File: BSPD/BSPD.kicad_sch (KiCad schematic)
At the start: 40 parts, among them J1 DT13-48PABCD-R015, K1 Latching Relay, Q1 STS6NF20V, U1 LM7805CT, U10 DK1A1B-12V, U12 LM555N, U2 NSL-32, U2 OP AMP, U3 OP AMP, U4 Inverter (Not Gate), U5 2x4 OR GATE, U6 LM555N, U8 NAND, U9 AND GATE

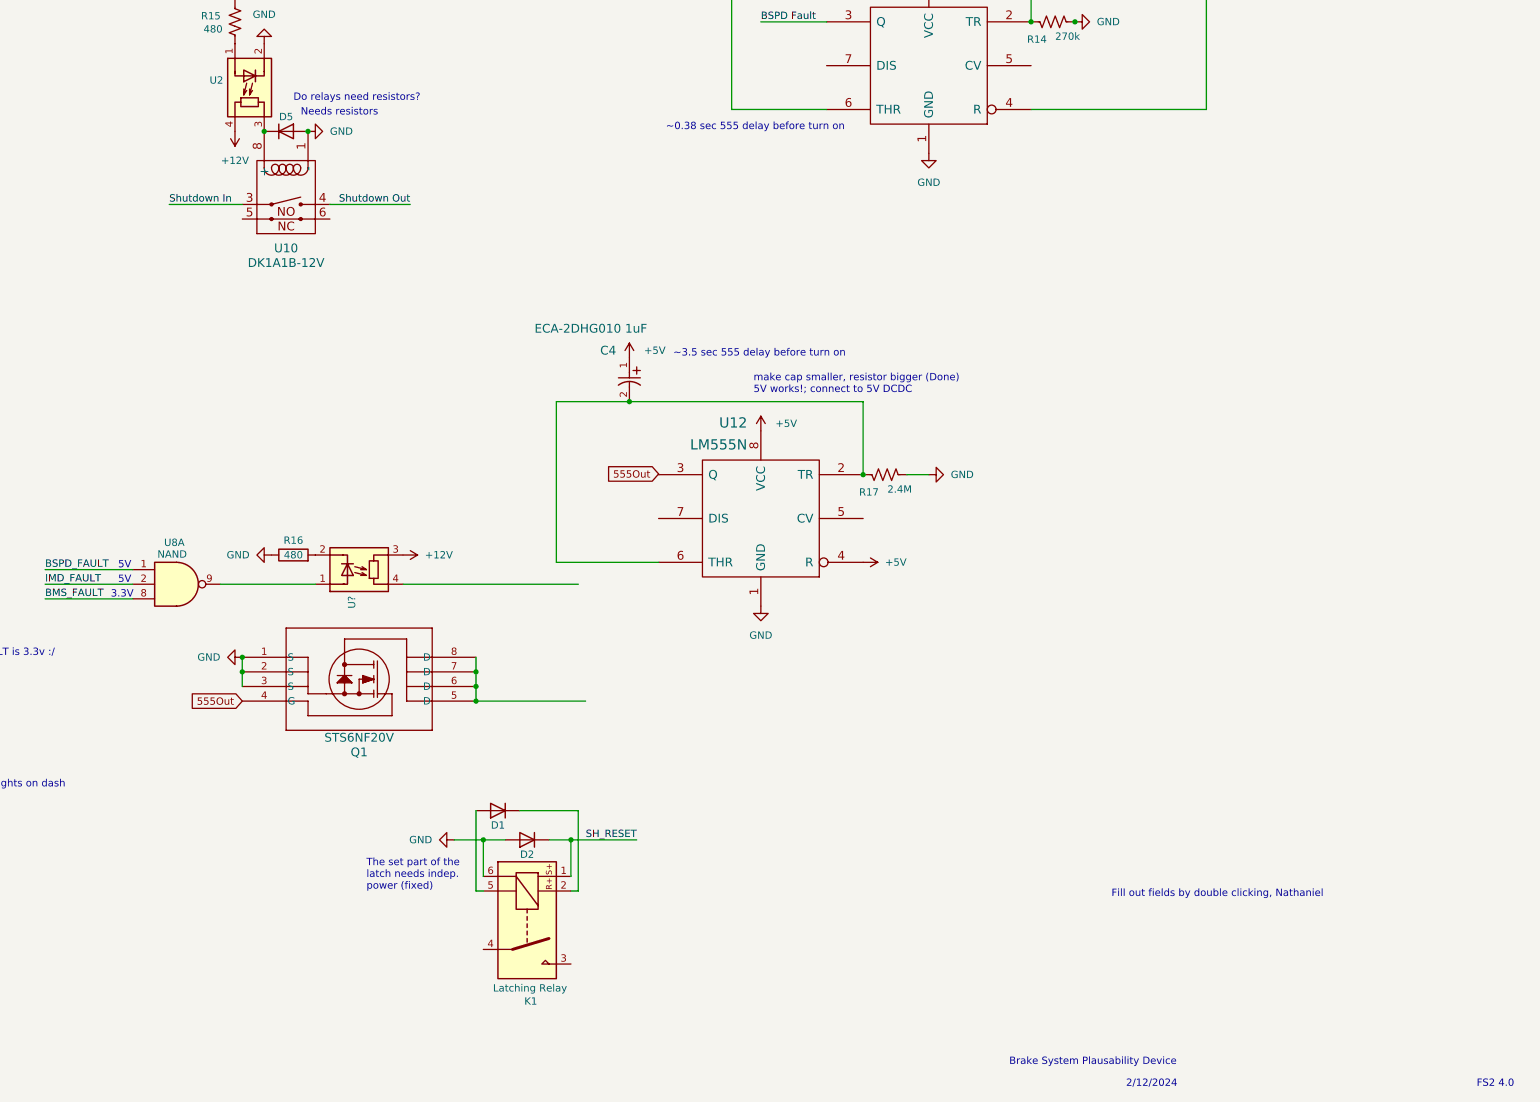
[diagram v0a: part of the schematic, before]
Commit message: Merge branch 'master' of github.com:formulaslug/fs-2-schematics
Updated title to be in title text rather than text
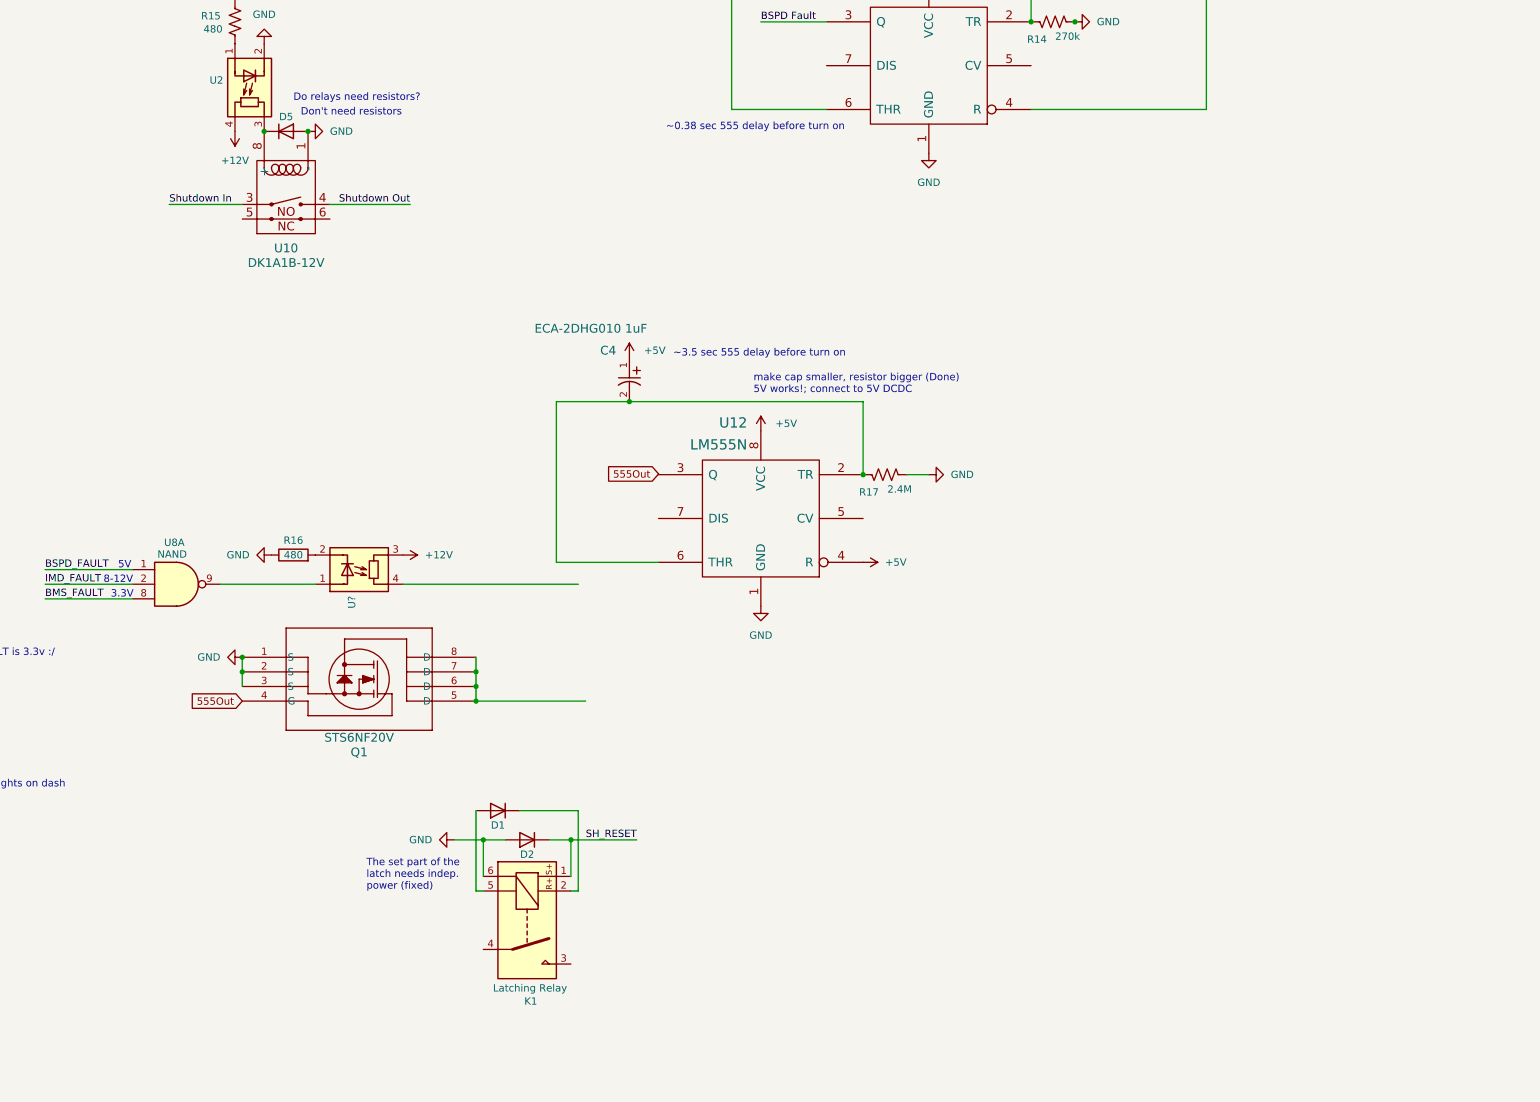
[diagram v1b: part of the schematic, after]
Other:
- note added: "8-12V"
- note added: "Don't need resistors"
- note removed: "2/12/2024"
- note removed: "Brake System Plausability Device"
- note removed: "FS2 4.0"
- note removed: "Fill out fields by double clicking, Nathaniel"
- note removed: "Needs resistors"
- title: (none) -> Brake System Plausability Device
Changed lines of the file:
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@@
 (kicad_sch (version 20230121) (generator eeschema)
   (paper "A3")
+  (title_block
+    (title "Brake System Plausability Device")
+    (date "2024-02-22")
+    (rev "FS2 4.1")
+  )
   (junction (at 45.72 34.29) (diameter 0) (color 0 0 0 0)
   )
@@
     (effects (font (size 1.27 1.27)) (justify left bottom))
   )
-  (text "Fill out fields by double clicking, Nathaniel" (at 326.39 247.65 0)
-    (effects (font (size 1.27 1.27)) (justify left bottom))
-  )
   (text "GLV" (at 46.101 145.796 0)
     (effects (font (size 1.27 1.27)) (justify left bottom))
@@
     (effects (font (size 1.27 1.27)) (justify left bottom))
   )
-  (text "5V" (at 153.67 193.04 0)
+  (text "8-12V" (at 151.13 193.04 0)
     (effects (font (size 1.27 1.27)) (justify left bottom))
   )
@@
     (effects (font (size 1.27 1.27)) (justify left bottom))
   )
-  (text "Needs resistors\n" (at 185.42 111.76 0)
-    (effects (font (size 1.27 1.27)) (justify left bottom))
-  )
-  (text "2/12/2024" (at 328.93 280.67 0)
+  (text "Don't need resistors\n" (at 185.42 111.76 0)
     (effects (font (size 1.27 1.27)) (justify left bottom))
   )
@@
     (effects (font (size 1.27 1.27)) (justify left bottom))
   )
-  (text "Brake System Plausability Device" (at 308.61 276.86 0)
-    (effects (font (size 1.27 1.27)) (justify left bottom))
-  )
   (text "GND" (at 46.101 148.336 0)
     (effects (font (size 1.27 1.27)) (justify left bottom))
@@
     (effects (font (size 1.27 1.27)) (justify left bottom))
   )
-  (text "FS2 4.0\n" (at 389.89 280.67 0)
-    (effects (font (size 1.27 1.27)) (justify left bottom))
-  )

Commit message: Update BSPD.kicad_sch
bspd upadtes
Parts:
- added C5, C6: C_Polarized, 1FS_2_Global_Footprint_Library:Basic 2 Hole, symbol Device:C_Polarized
- added U13: LM7805CT, 1FS_2_Global_Footprint_Library:Basic 3 Hole, symbol Regulator_Linear:LM317_TO-252
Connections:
- net GND: now also C5.2, C6.2, U13.1 (ADJ)
- net IMD_FAULT: now also C5.1, U13.3 (VI); no longer U8.2
- new net: C6.1, U13.2 (VO), U8.2
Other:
- note added: "IMD_FAULT 5V"
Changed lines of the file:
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@@
     (rev "FS2 4.1")
   )
+  (junction (at 93.98 193.04) (diameter 0) (color 0 0 0 0)
+  )
   (junction (at 45.72 34.29) (diameter 0) (color 0 0 0 0)
   )
@@
   )
   (junction (at 320.04 95.25) (diameter 0) (color 0 0 0 0)
+  )
+  (junction (at 115.57 193.04) (diameter 0) (color 0 0 0 0)
+  )
+  (junction (at 104.14 200.66) (diameter 0) (color 0 0 0 0)
   )
   (junction (at 298.45 71.12) (diameter 0) (color 0 0 0 0)
@@
     (stroke (width 0) (type default))
   )
-  (wire (pts (xy 140.97 193.04) (xy 156.21 193.04))
+  (wire (pts (xy 115.57 193.04) (xy 156.21 193.04))
     (stroke (width 0) (type default))
   )
@@
     (stroke (width 0) (type default))
   )
+  (wire (pts (xy 74.93 193.04) (xy 93.98 193.04))
+    (stroke (width 0) (type default))
+  )
   (wire (pts (xy 220.98 237.49) (xy 217.17 237.49))
     (stroke (width 0) (type default))
@@
     (stroke (width 0) (type default))
   )
+  (wire (pts (xy 111.76 193.04) (xy 115.57 193.04))
+    (stroke (width 0) (type default))
+  )
   (wire (pts (xy 215.9 213.36) (xy 234.95 213.36))
     (stroke (width 0) (type default))
@@
     (stroke (width 0) (type default))
   )
+  (wire (pts (xy 93.98 193.04) (xy 96.52 193.04))
+    (stroke (width 0) (type default))
+  )
   (wire (pts (xy 265.43 95.25) (xy 276.86 95.25))
     (stroke (width 0) (type default))
@@
     (stroke (width 0) (type default))
   )
+  (wire (pts (xy 104.14 200.66) (xy 115.57 200.66))
+    (stroke (width 0) (type default))
+  )
   (wire (pts (xy 204.47 127) (xy 190.5 127))
     (stroke (width 0) (type default))
@@
   )
   (wire (pts (xy 164.211 67.31) (xy 167.64 67.31))
+    (stroke (width 0) (type default))
+  )
+  (wire (pts (xy 93.98 200.66) (xy 104.14 200.66))
     (stroke (width 0) (type default))
   )
@@
     (effects (font (size 1.27 1.27)) (justify left bottom))
   )
-  (text "8-12V" (at 151.13 193.04 0)
+  (text "8-12V" (at 86.36 193.04 0)
     (effects (font (size 1.27 1.27)) (justify left bottom))
   )
@@
     (effects (font (size 1.27 1.27)) (justify left bottom))
   )
-  (text "BMS_FAULT is 3.3v :/" (at 124.46 205.74 0)
-    (effects (font (size 1.27 1.27)) (justify left bottom))
-  )
-  (text "Current Sensor\nOpen Circuit\n" (at 97.79 121.92 0)
+  (text "BMS_FAULT is 3.3v :/" (at 137.16 198.12 0)
+    (effects (font (size 1.27 1.27)) (justify left bottom))
+  )
+  (text "Current Sensor\nOpen Circuit\n" (at 92.71 127 0)
     (effects (font (size 1.27 1.27)) (justify left bottom))
   )
@@
   )
   (text "BSPD delay (0.5 sec)" (at 300.99 74.93 0)
+    (effects (font (size 1.27 1.27)) (justify left bottom))
+  )
+  (text "IMD_FAULT 5V" (at 118.11 193.04 0)
+    (effects (font (size 1.27 1.27)) (justify left bottom))
+  )
+  (text "IMD_FAULT 5V" (at 142.24 193.04 0)
     (effects (font (size 1.27 1.27)) (justify left bottom))
   )
@@
     (effects (font (size 1.27 1.27)) (justify left bottom))
   )
-  (label "IMD_FAULT" (at 140.97 193.04 0) (fields_autoplaced)
-    (effects (font (size 1.27 1.27)) (justify left bottom))
-  )
   (label "BSPD_FAULT" (at 140.97 190.5 0) (fields_autoplaced)
+    (effects (font (size 1.27 1.27)) (justify left bottom))
+  )
+  (label "IMD_FAULT" (at 74.93 193.04 0) (fields_autoplaced)
     (effects (font (size 1.27 1.27)) (justify left bottom))
   )
@@
     )
   )
+  (symbol (lib_id "power:GND") (at 104.14 200.66 0) (unit 1)
+    (in_bom yes) (on_board yes) (dnp no) (fields_autoplaced)
+    (property "Reference" "#PWR042" (at 104.14 207.01 0)
+      (effects (font (size 1.27 1.27)) hide)
+    )
+    (property "Value" "GND" (at 104.14 205.74 0)
+      (effects (font (size 1.27 1.27)))
+    )
+    (property "Footprint" "" (at 104.14 200.66 0)
+      (effects (font (size 1.27 1.27)) hide)
+    )
+    (property "Datasheet" "" (at 104.14 200.66 0)
+      (effects (font (size 1.27 1.27)) hide)
+    )
+    (pin "1")
+    (instances
+      (project "BSPD"
+        (path "/9b958334-fa88-4811-8197-71444a07b1b5"
+          (reference "#PWR042") (unit 1)
+        )
+      )
+    )
+  )
   (symbol (lib_id "Regulator_Linear:LM317_TO-252") (at 34.29 34.29 0) (unit 1)
     (in_bom yes) (on_board yes) (dnp no) (fields_autoplaced)
@@
     )
   )
+  (symbol (lib_id "Regulator_Linear:LM317_TO-252") (at 104.14 193.04 0) (unit 1)
+    (in_bom yes) (on_board yes) (dnp no) (fields_autoplaced)
+    (property "Reference" "U13" (at 104.14 186.69 0)
+      (effects (font (size 1.27 1.27)))
+    )
+    (property "Value" "LM7805CT" (at 104.14 189.23 0)
+      (effects (font (size 1.27 1.27)))
+    )
+    (property "Footprint" "1FS_2_Global_Footprint_Library:Basic 3 Hole" (at 104.14 186.69 0)
+      (effects (font (size 1.27 1.27) italic) hide)
+    )
+    (property "Datasheet" "https://www.ti.com/lit/ds/symlink/lm7800.pdf" (at 104.14 193.04 0)
+      (effects (font (size 1.27 1.27)) hide)
+    )
+    (pin "1")
+    (pin "2")
+    (pin "3")
+    (instances
+      (project "BSPD"
+        (path "/9b958334-fa88-4811-8197-71444a07b1b5"
+          (reference "U13") (unit 1)
+        )
+      )
+    )
+  )
   (symbol (lib_id "Device:R_US") (at 35.56 93.98 270) (unit 1)
     (in_bom yes) (on_board yes) (dnp no)
@@
         (path "/e19d26dd-723b-45e6-9d59-b1730158e759"
           (reference "#PWR024") (unit 1)
+        )
+      )
+    )
+  )
+  (symbol (lib_id "Device:C_Polarized") (at 93.98 196.85 0) (unit 1)
+    (in_bom yes) (on_board yes) (dnp no)
+    (property "Reference" "C5" (at 88.9 199.39 0)
+      (effects (font (size 1.27 1.27)) (justify left))
+    )
+    (property "Value" "C_Polarized" (at 88.9 201.93 0)
+      (effects (font (size 1.27 1.27)) (justify left))
+    )
+    (property "Footprint" "1FS_2_Global_Footprint_Library:Basic 2 Hole" (at 94.9452 200.66 0)
+      (effects (font (size 1.27 1.27)) hide)
+    )
+    (property "Datasheet" "~" (at 93.98 196.85 0)
+      (effects (font (size 1.27 1.27)) hide)
+    )
+    (pin "1")
+    (pin "2")
+    (instances
+      (project "BSPD"
+        (path "/9b958334-fa88-4811-8197-71444a07b1b5"
+          (reference "C5") (unit 1)
         )
       )
@@
         )
       )
+    )
+  )
+  (symbol (lib_id "Device:C_Polarized") (at 115.57 196.85 0) (unit 1)
+    (in_bom yes) (on_board yes) (dnp no) (fields_autoplaced)
+    (property "Reference" "C6" (at 119.38 194.691 0)
+      (effects (font (size 1.27 1.27)) (justify left))
+    )
+    (property "Value" "C_Polarized" (at 119.38 197.231 0)
+      (effects (font (size 1.27 1.27)) (justify left))
+    )
+    (property "Footprint" "1FS_2_Global_Footprint_Library:Basic 2 Hole" (at 116.5352 200.66 0)
+      (effects (font (size 1.27 1.27)) hide)
+    )
+    (property "Datasheet" "~" (at 115.57 196.85 0)
+      (effects (font (size 1.27 1.27)) hide)
+    )
+    (pin "1")
+    (pin "2")
+    (instances
+      (project "BSPD"
+        (path "/9b958334-fa88-4811-8197-71444a07b1b5"
+          (reference "C6") (unit 1)
+        )
+      )

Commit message: Updated for Mosfet, latching, and dash lights
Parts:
- removed CR2: STS6NF20V, 1FS_2_Global_Footprint_Library:SO-8_STM, symbol 1_ACC_BOARD:STS6NF20V
- removed R13: 8.2k, Resistor_THT:R_Axial_DIN0207_L6.3mm_D2.5mm_P10.16mm_Horizontal, symbol Device:R_US
- removed R16: 480, symbol Device:R
- removed R7: 100k, Resistor_THT:R_Axial_DIN0207_L6.3mm_D2.5mm_P10.16mm_Horizontal, symbol Device:R_US
- added Q2, Q3: STS6NF20V, 1FS_2_Global_Footprint_Library:SO-8_STM, symbol 1_ACC_BOARD:STS6NF20V
- C3: footprint PCAP_63x112_PAN -> 1FS_2_Global_Footprint_Library:PCAP_63x112_PAN
- R1: value 20k -> 39k; footprint Resistor_THT:R_Axial_DIN0207_L6.3mm_D2.5mm_P10.16mm_Horizontal -> Resistor_SMD:R_0805_2012Metric_Pad1.20x1.40mm_HandSolder
- R10: value 100k -> 330k; footprint Resistor_THT:R_Axial_DIN0207_L6.3mm_D2.5mm_P10.16mm_Horizontal -> Resistor_SMD:R_0805_2012Metric_Pad1.20x1.40mm_HandSolder
- R11: value 3k -> 39k; footprint Resistor_THT:R_Axial_DIN0207_L6.3mm_D2.5mm_P10.16mm_Horizontal -> Resistor_SMD:R_0805_2012Metric_Pad1.20x1.40mm_HandSolder
- R12: value 22k -> 15k; footprint Resistor_THT:R_Axial_DIN0207_L6.3mm_D2.5mm_P10.16mm_Horizontal -> Resistor_SMD:R_0805_2012Metric_Pad1.20x1.40mm_HandSolder
- R14, R3: footprint Resistor_THT:R_Axial_DIN0207_L6.3mm_D2.5mm_P10.16mm_Horizontal -> Resistor_SMD:R_0805_2012Metric_Pad1.20x1.40mm_HandSolder
- R15: value 480 -> 470; footprint Resistor_THT:R_Axial_DIN0207_L6.3mm_D2.5mm_P10.16mm_Horizontal -> Resistor_SMD:R_0805_2012Metric_Pad1.20x1.40mm_HandSolder
- R17: footprint (none) -> Resistor_SMD:R_0805_2012Metric_Pad1.20x1.40mm_HandSolder
- R2: value 10k -> 18k; footprint Resistor_THT:R_Axial_DIN0207_L6.3mm_D2.5mm_P10.16mm_Horizontal -> Resistor_SMD:R_0805_2012Metric_Pad1.20x1.40mm_HandSolder
- R4: value 22k -> 18k; footprint Resistor_THT:R_Axial_DIN0207_L6.3mm_D2.5mm_P10.16mm_Horizontal -> Resistor_SMD:R_0805_2012Metric_Pad1.20x1.40mm_HandSolder
- R5: value 100k -> 82k; footprint Resistor_THT:R_Axial_DIN0207_L6.3mm_D2.5mm_P10.16mm_Horizontal -> Resistor_SMD:R_0805_2012Metric_Pad1.20x1.40mm_HandSolder
- R6: value 75k -> 470; footprint Resistor_THT:R_Axial_DIN0207_L6.3mm_D2.5mm_P10.16mm_Horizontal -> Resistor_SMD:R_0805_2012Metric_Pad1.20x1.40mm_HandSolder
- R8: value 11k -> 330k; footprint Resistor_THT:R_Axial_DIN0207_L6.3mm_D2.5mm_P10.16mm_Horizontal -> Resistor_SMD:R_0805_2012Metric_Pad1.20x1.40mm_HandSolder
- R9: value 100k -> 10k; footprint Resistor_THT:R_Axial_DIN0207_L6.3mm_D2.5mm_P10.16mm_Horizontal -> Resistor_SMD:R_0805_2012Metric_Pad1.20x1.40mm_HandSolder
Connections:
- net BMS_FAULT is gone; now on net BMS_FAULT 5V: U8.8
- net +12V: now also U?.4 (R); no longer U?.3 (R)
- net +5V: now also R1.1, R9.2; no longer R12.1, R8.1
- net 4.5V: now also R1.2, R8.1; no longer R8.2, R9.1
- net GND: now also J1.D1, R11.2, R12.1, R3.1, R6.1, R8.2, Q2.1 (S), Q2.2 (S), Q2.3 (S), Q3.1 (S), Q3.2 (S), Q3.3 (S); no longer J1.A2, R1.1, R9.2
- net IMD_FAULT: now also J1.A9
- net SH_RESET: now also J1.A6
- net Shutdown In: now also J1.A8; no longer J1.A5
- net Shutdown Out: now also J1.D3, K1.3; no longer J1.A6, U10.4
- net at C3.1, U6.4 (R), U6.8 (VCC): now also U4.4
- net BMS_FAULT 3.3V: now reaches U3.10
- net BMS_FAULT 3.3V: now also J1.A10
- net BMS_FAULT 5V: now reaches U3.8
- net BMS_FAULT 5V: now also Q2.4 (G)
- net 3V: now reaches U3.9
- net 3V: now also R12.2, R9.1
- net at D1.1 (K), K1.2: now also Q1.5 (D), Q1.6 (D), Q1.7 (D), Q1.8 (D)
- net at D1.2 (A), K1.5: now also U?.3 (R)
- net at K1.4: now also U10.4
- net IMD_FAULT 5V: now reaches C6.1, U13.2 (VO), U8.2
- net IMD_FAULT 5V: now also Q3.4 (G)
- net at U?.2 (K): now also R6.2
- net BMS Light Low Side: now reaches J1.A11
- net BMS Light Low Side: now also Q2.5 (D), Q2.6 (D), Q2.7 (D), Q2.8 (D)
- net IMD Light Low Side: now reaches J1.A12
- net IMD Light Low Side: now also Q3.5 (D), Q3.6 (D), Q3.7 (D), Q3.8 (D)
- net 2.53V renamed Current Vref
- net Current Vref: now also J1.A5; no longer R6.2
- net 555Out renamed IMD Latch Delay
- net Brk renamed Brake Output
- net CrS renamed Current Output
- no-connect marks 5 -> 43
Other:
- note added: "IMD and BMS Lights"
- note removed: "3.3V"
- note removed: "BMS_FAULT is 3.3v :/"
- note removed: "Brk"
- note removed: "CrS"
- note removed: "GLV"
- note removed: "GND"
- note removed: "IMD_FAULT 5V"
- note removed: "Power IMD and BMS lights on dash"
- note removed: "Rst"
- note removed: "Sh+"
- note removed: "Sh-"
- moved on the sheet: C3, C4, C5, C6, D1, D2, D5, K1, Q1, R10, R11, R14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

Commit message: updating BSPD more
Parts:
- removed C1, C2, C5, C6: C_Polarized, 1FS_2_Global_Footprint_Library:Basic 2 Hole, symbol Device:C_Polarized
- removed C3, C4: ECA-2DHG010 1uF, 1FS_2_Global_Footprint_Library:PCAP_63x112_PAN, symbol 1FS_2_Global_Symbol_Library:ECA-2DHG010
- added C1, C7: 330nf, symbol Device:C
- added C2, C8: 100nf, symbol Device:C
- added C3, C5: 1uf, symbol Device:C
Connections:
- net +12V: now also C1.1
- net +5V: now also C2.1, C5.1
- net BSPD Fault: no longer J1.A7
- net GND: now also C1.2, C2.2, C7.2, C8.2
- net IMD_FAULT: now also C7.1
- net IMD_FAULT 5V: now also C8.1
- net at U4.4, U6.4 (R), U6.8 (VCC): now also C3.1
- net at R14.1, U6.2 (TR), U6.6 (THR): now also C3.2
- net at R17.1, U12.2 (TR), U12.6 (THR): now also C5.2
- no-connect marks 43 -> 45
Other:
- moved on the sheet: R14, R17, U12, U6
